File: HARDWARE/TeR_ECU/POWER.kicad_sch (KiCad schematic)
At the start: 5 parts, among them U2 TSR_1-2450

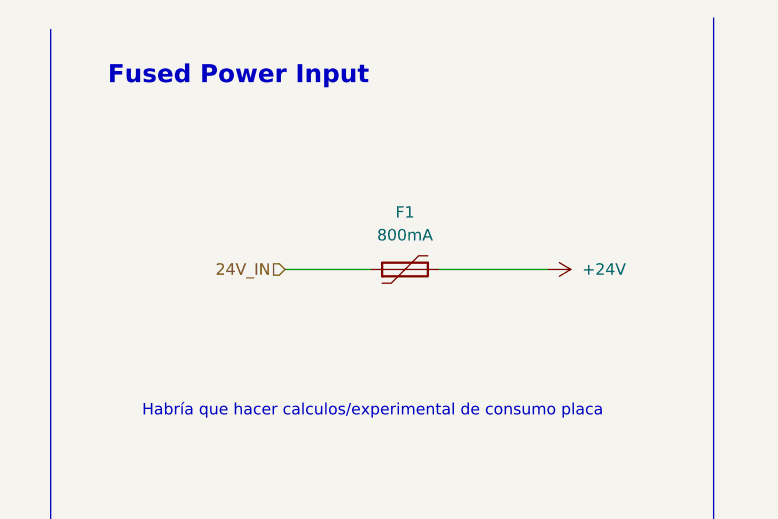
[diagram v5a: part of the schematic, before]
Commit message: Cambiado valor fusible
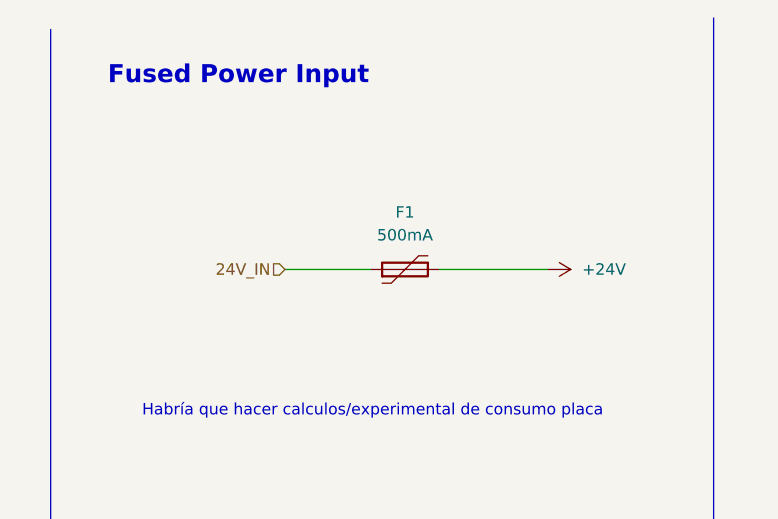
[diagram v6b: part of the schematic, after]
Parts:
- F1: value 800mA -> 500mA
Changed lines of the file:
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@@
       (effects (font (size 1.27 1.27)))
     )
-    (property "Value" "800mA" (at 165.1 35.56 90)
+    (property "Value" "500mA" (at 165.1 35.56 90)
       (effects (font (size 1.27 1.27)))
     )

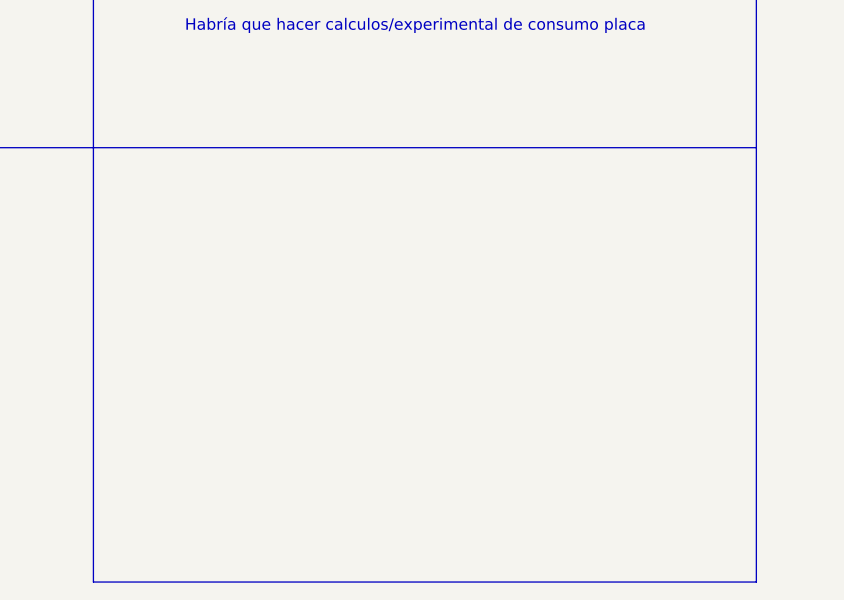
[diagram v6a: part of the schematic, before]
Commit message: Microcontroller f405 sketch started
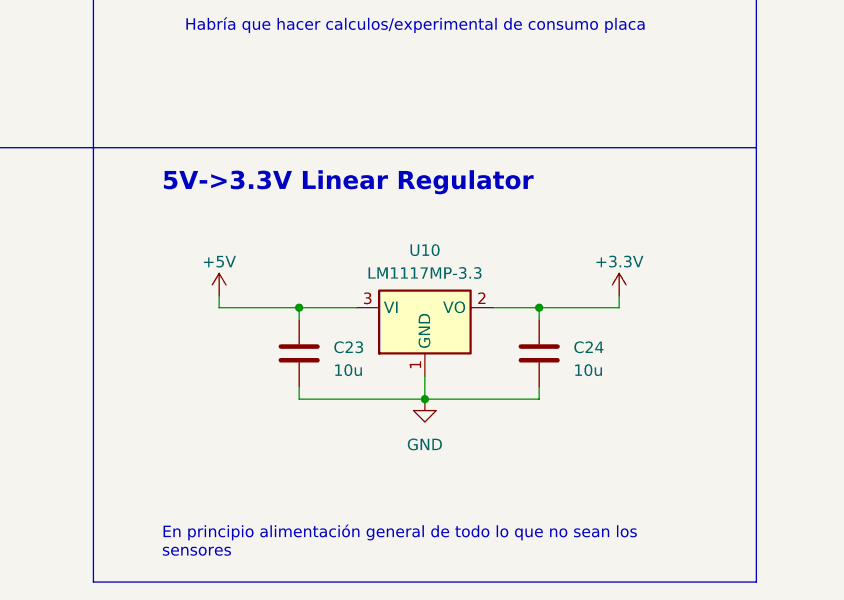
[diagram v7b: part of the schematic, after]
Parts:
- added C23, C24: 10u, Capacitor_SMD:C_0603_1608Metric, symbol Device:C
- added U10: LM1117MP-3.3, Package_TO_SOT_SMD:SOT-223-3_TabPin2, symbol Regulator_Linear:LM1117MP-3.3
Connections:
- net +5V: now also C23.1, U10.3 (VI)
- net GND: now also C23.2, C24.2, U10.1 (GND)
- new net +3.3V: C24.1, U10.2 (VO)
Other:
- note added: "5V->3.3V Linear Regulator"
- note added: "En principio alimentación general de todo lo que no sean los sensores"

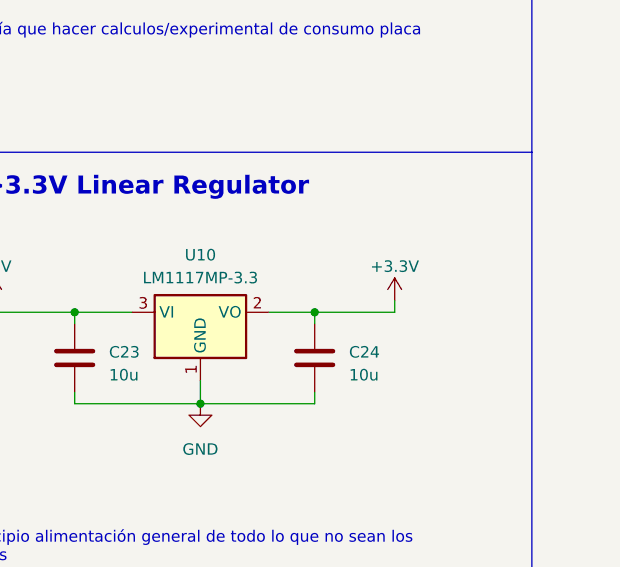
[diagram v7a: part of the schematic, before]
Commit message: usb-c, good debug conn, switch
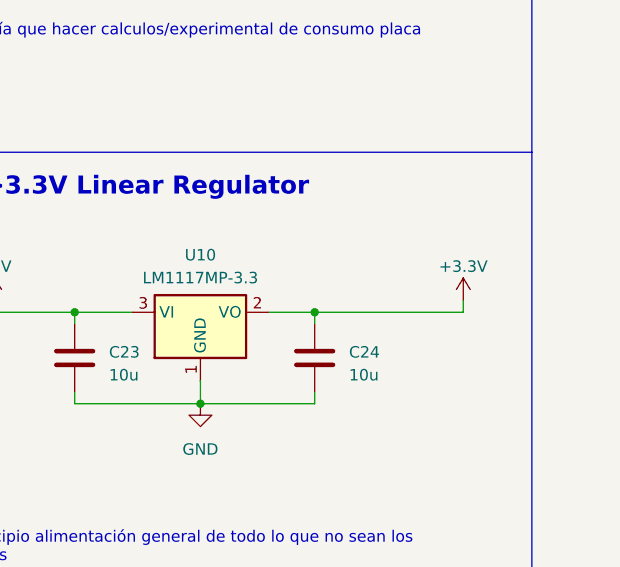
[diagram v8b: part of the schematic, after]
